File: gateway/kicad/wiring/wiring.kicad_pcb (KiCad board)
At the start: 2 copper layers, 6 parts, among them J1 Conn_01x01_Male, J2 BME280, U1 ARDUINO_PRO_MINI, U2 nRF24L01+

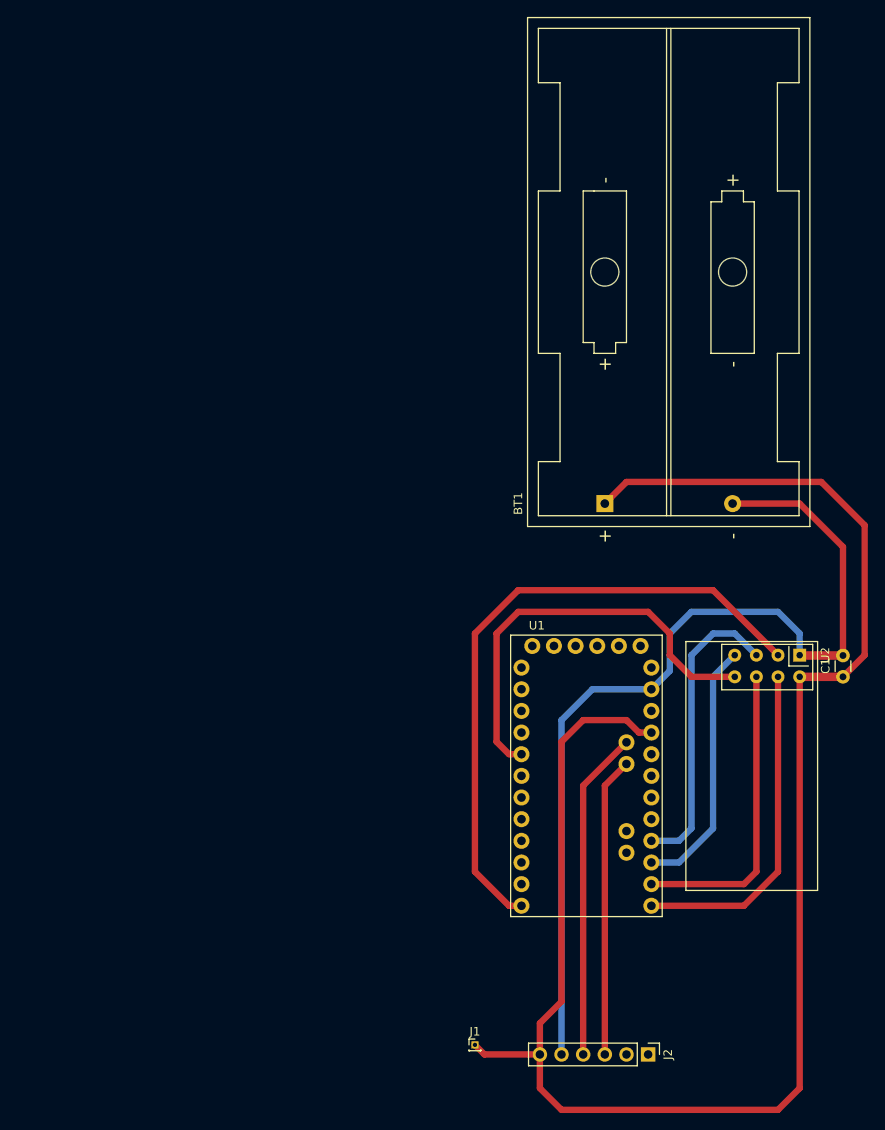
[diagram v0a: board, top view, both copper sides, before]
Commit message: feat: wiring for gateway
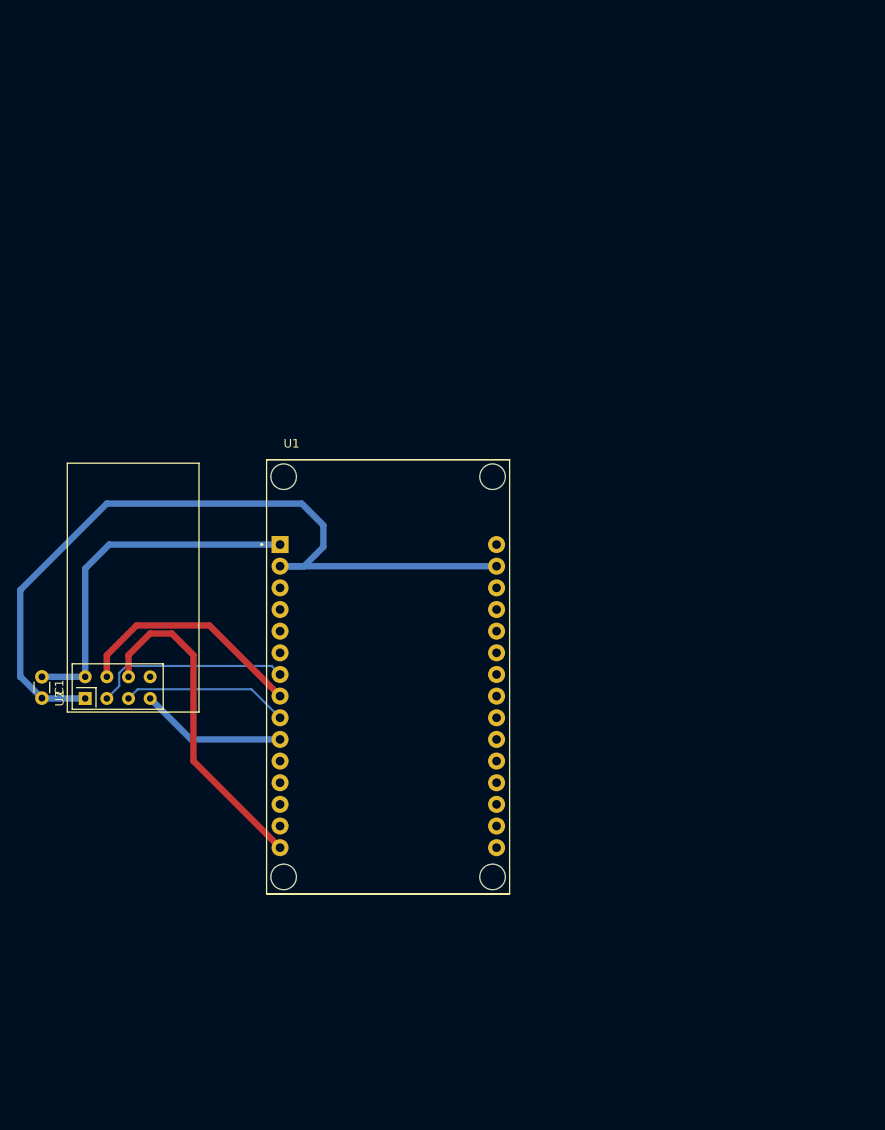
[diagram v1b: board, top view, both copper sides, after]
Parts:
- removed BT1: 2x1,5V, Battery:BatteryHolder_Keystone_2462_2xAA
- removed J1: Conn_01x01_Male, Connector_PinHeader_1.00mm:PinHeader_1x01_P1.00mm_Vertical
- removed J2: BME280, Connector_PinHeader_2.54mm:PinHeader_1x06_P2.54mm_Vertical
- U1: value ARDUINO_PRO_MINI -> ESP32-DEVKIT-V1; footprint ARDUINO_PRO_MINI:MODULE_ARDUINO_PRO_MINI -> ESP32-DEVKIT-V1:MODULE_ESP32_DEVKIT_V1
- moved C1 94.0 mm to (73.7, 96.5), turned to -90 degrees
- moved U2 84.0 mm to (78.7, 99.1), turned to 90 degrees
- moved U1 26.0 mm to (114.3, 96.5)
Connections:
- C1 pad 1: Net-(U1-PadJP6_4) -> Net-(U1-Pad1)
- C1 pad 2: GND -> Net-(U2-Pad1)
- U2 pad 1: GND -> Net-(U2-Pad1)
- U2 pad 2: Net-(U1-PadJP6_4) -> Net-(U1-Pad1)
- U2 pad 3: Net-(U1-PadJP7_1) -> Net-(U2-Pad3)
- U2 pad 4: Net-(U1-PadJP6_12) -> Net-(U2-Pad4)
- U2 pad 5: Net-(U1-PadJP6_9) -> Net-(U2-Pad5)
- U2 pad 6: Net-(U1-PadJP6_11) -> Net-(U1-Pad15)
- U2 pad 7: Net-(U1-PadJP6_10) -> Net-(U1-Pad10)
- U2 pad 8: Net-(U1-PadJP7_8) -> unconnected-(U2-Pad8)
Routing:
- net Net-(U1-PadJP6_4): track 200.4 -> 0.00 mm
- net GND: track 111.5 -> 0.00 mm
- net Net-(U2-Pad1): track 0.00 -> 93.6 mm
- net Net-(U1-PadJP7_1): track 75.9 -> 0.00 mm
- net Net-(U1-PadJP7_8): track 49.9 -> 0.00 mm
- net Net-(U1-Pad1): track 0.00 -> 41.8 mm
- net Net-(U1-PadJP6_12): track 39.4 -> 0.00 mm
- net Net-(U1-Pad15): track 0.00 -> 39.1 mm
- net Net-(U1-PadJP2_2): track 38.7 -> 0.00 mm
- net Net-(U1-PadJP6_11): track 35.8 -> 0.00 mm
- net Net-(U1-PadJP6_9): track 35.3 -> 0.00 mm
- net Net-(U1-PadJP2_1): track 35.1 -> 0.00 mm
- net Net-(U1-PadJP6_10): track 30.3 -> 0.00 mm
- net Net-(U2-Pad4): track 0.00 -> 27.7 mm
- net Net-(U2-Pad3): track 0.00 -> 23.2 mm
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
